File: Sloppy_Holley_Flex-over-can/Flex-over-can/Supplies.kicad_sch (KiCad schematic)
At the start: 7 parts, among them U11 ME6211C33M5G-N, U3 TPS7B6950QDCYRQ1

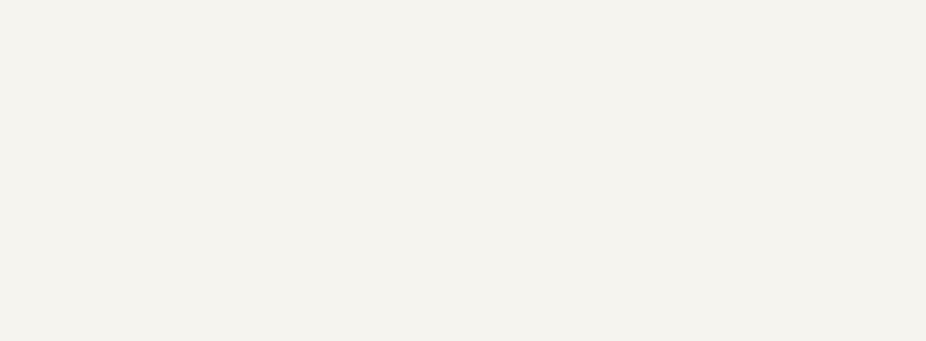
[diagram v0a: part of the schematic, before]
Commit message: Add PCB placement notes for decoupling caps to each sheet
Co-Authored-By: Claude Opus 5.5 <noreply@anthropic.com>
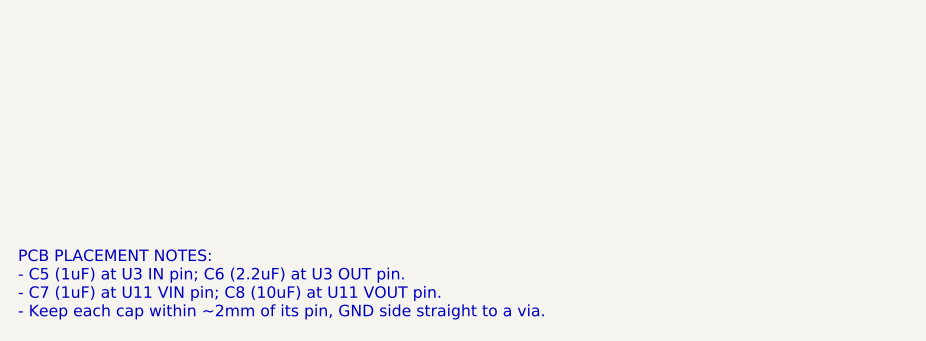
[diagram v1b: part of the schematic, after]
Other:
- note added: "PCB PLACEMENT NOTES: - C5 (1uF) at U3 IN pin; C6 (2.2uF) at U3 OUT pin. - C7 (1uF) at U11 VIN pin; C8 (10uF) at U11 VOUT pin. - Keep each cap within ~2mm of its pin, GND side straight to a via."
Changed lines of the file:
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@@
 		)
 	)
+  (text "PCB PLACEMENT NOTES:\n- C5 (1uF) at U3 IN pin; C6 (2.2uF) at U3 OUT pin.\n- C7 (1uF) at U11 VIN pin; C8 (10uF) at U11 VOUT pin.\n- Keep each cap within ~2mm of its pin, GND side straight to a via."
+    (at 15.24 180.34 0)
+    (effects (font (size 1.27 1.27) (color 0 0 194 1)) (justify left bottom))
+  )
 	(symbol
 		(lib_id "FlexCAN:TPS7B6950QDCY")
